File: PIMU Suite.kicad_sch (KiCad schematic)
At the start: 5 parts, among them J1 Conn_01x05, U1 Teensy4.1, U2 MICROSD_SPI_OR_SDIO_CARD

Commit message: Added impl note
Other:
- note added: "Note: Adafruit labeled this as 3V when its really 3.3V"
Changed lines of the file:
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@@
+		)
+	)
+	(text "Note: Adafruit labeled this \nas 3V when its really 3.3V"
+		(exclude_from_sim no)
+		(at 114.046 37.084 0)
+		(effects
+			(font
+				(size 1.27 1.27)
+			)
 		)
 	)

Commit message: Change pwer dist.
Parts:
- removed J1: Conn_01x05, Connector_PinHeader_1.00mm:PinHeader_1x05_P1.00mm_Vertical, symbol Connector_Generic:Conn_01x05
- added D1: LED, LED_THT:LED_D3.0mm, symbol Device:LED
- added R1: R_US, Resistor_THT:R_Axial_DIN0207_L6.3mm_D2.5mm_P7.62mm_Horizontal, symbol Device:R_US
- added TP1: 5V IN, TestPoint:TestPoint_Pad_D1.5mm, symbol Connector:TestPoint
- added TP2: GND CONN, TestPoint:TestPoint_Pad_D1.5mm, symbol Connector:TestPoint
- added TP3: I2C CLOCK, TestPoint:TestPoint_Pad_D1.5mm, symbol Connector:TestPoint
- added TP4: I2C DATA, TestPoint:TestPoint_Pad_D1.5mm, symbol Connector:TestPoint
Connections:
- net at BMP1.4 (SCK), IMU1.10 (SCL), U1.41 (19_A5_SCL): now also TP3.1
- net at IMU1.11 (SDA), U1.40 (18_A4_SDA): now also BMP1.5 (SDO), TP4.1; no longer BMP1.6 (SDI)
- net 3V3 IN: now reaches BMP1.1 (VIN), IMU1.7 (VIN), U1.46 (3V3), U2.1 (3V)
- net 3V3 IN: now also R1.2
- net GND: now reaches BMP1.3 (GND), IMU1.9 (GND), U1.1 (GND), U2.2 (GND)
- net GND: now also D1.1 (K), TP2.1
- net 5V TEENSY: now reaches U1.48 (VIN)
- net 5V TEENSY: now also TP1.1
- new net: D1.2 (A), R1.1
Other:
- note removed: "This is so we can test the teensy when not plugged into USB"
- moved on the sheet: U2

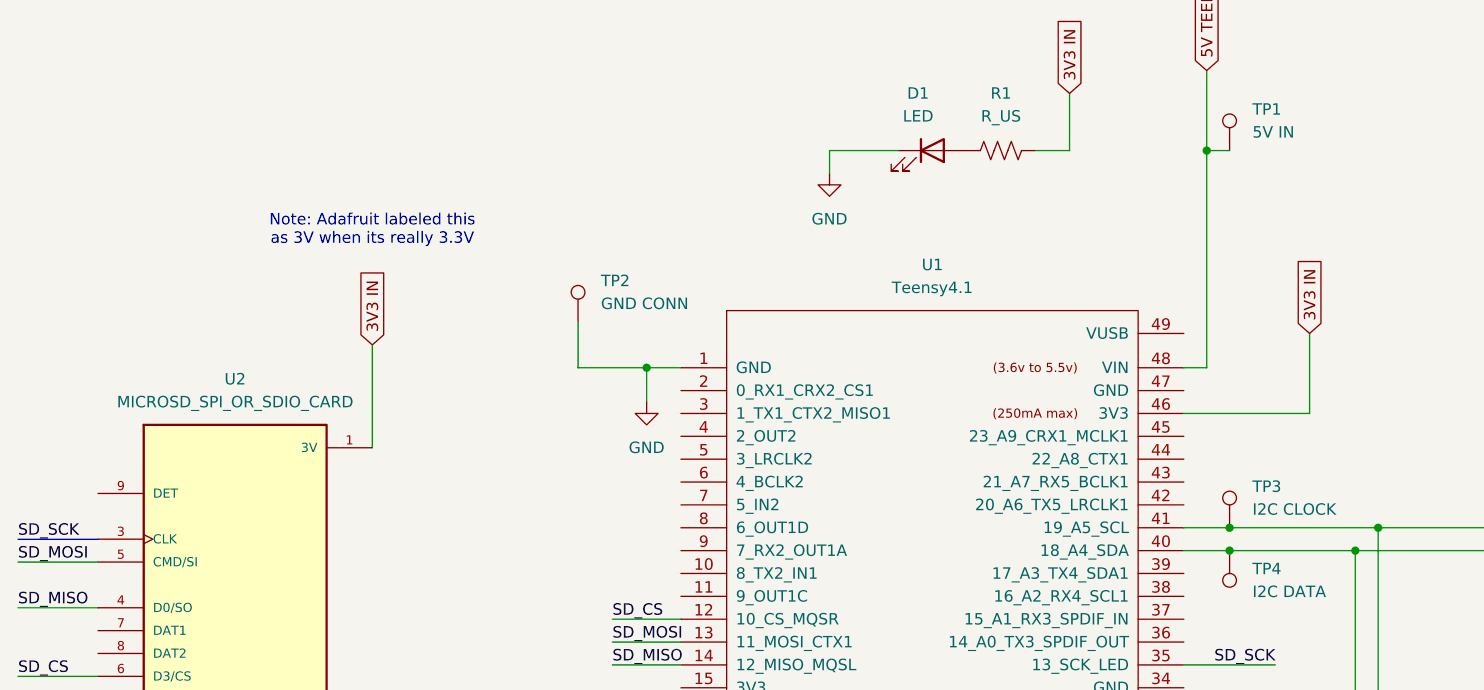
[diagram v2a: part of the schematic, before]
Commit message: Fix mistake from prev
also added a wire for the detect pin
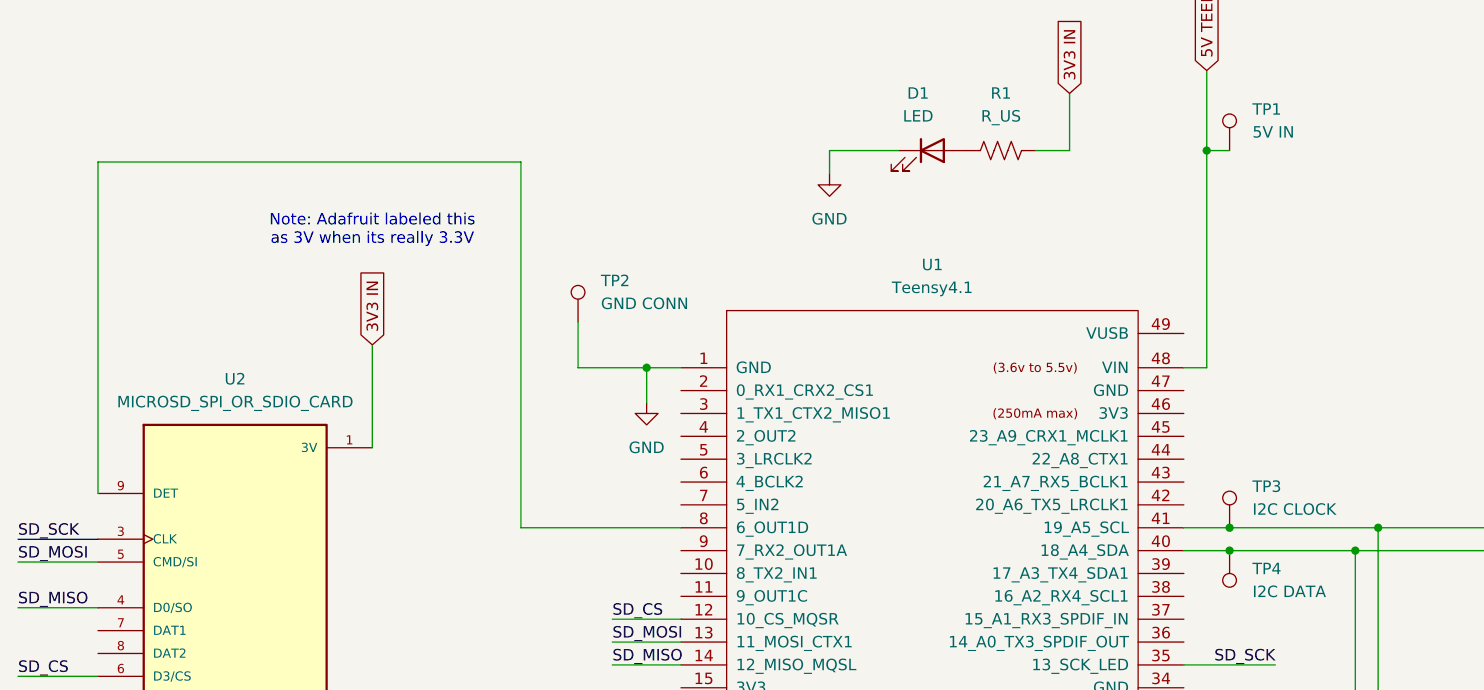
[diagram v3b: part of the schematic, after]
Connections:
- net 3V3 IN: no longer U1.46 (3V3)
- net at U1.8 (6_OUT1D): now also U2.9 (DET)
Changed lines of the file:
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@@
+	(wire
+		(pts
+			(xy 52.07 36.83) (xy 52.07 73.66)
+		)
+		(stroke
+			(width 0)
+			(type default)
+		)
+	)
 	(wire
 		(pts
@@
 	(wire
 		(pts
+			(xy 99.06 77.47) (xy 99.06 36.83)
+		)
+		(stroke
+			(width 0)
+			(type default)
+		)
+	)
+	(wire
+		(pts
 			(xy 194.31 77.47) (xy 194.31 104.14)
 		)
@@
 	(wire
 		(pts
-			(xy 172.72 64.77) (xy 186.69 64.77)
-		)
-		(stroke
-			(width 0)
-			(type default)
-		)
-	)
-	(wire
-		(pts
 			(xy 191.77 80.01) (xy 191.77 106.68)
 		)
@@
 	(wire
 		(pts
+			(xy 99.06 36.83) (xy 52.07 36.83)
+		)
+		(stroke
+			(width 0)
+			(type default)
+		)
+	)
+	(wire
+		(pts
 			(xy 43.18 86.36) (xy 52.07 86.36)
 		)
@@
 	(wire
 		(pts
+			(xy 116.84 77.47) (xy 99.06 77.47)
+		)
+		(stroke
+			(width 0)
+			(type default)
+		)
+	)
+	(wire
+		(pts
 			(xy 105.41 59.69) (xy 113.03 59.69)
 		)
@@
 		(pts
 			(xy 232.41 99.06) (xy 243.84 99.06)
-		)
-		(stroke
-			(width 0)
-			(type default)
-		)
-	)
-	(wire
-		(pts
-			(xy 186.69 55.88) (xy 186.69 64.77)
 		)
 		(stroke
@@
 			(effects
 				(font
-					(size 1.27 1.27)
-				)
-				(justify left)
-				(hide yes)
-			)
-		)
-	)
-	(global_label "3V3 IN"
-		(shape input)
-		(at 186.69 55.88 90)
-		(fields_autoplaced yes)
-		(effects
-			(font
-				(size 1.27 1.27)
-			)
-			(justify left)
-		)
-		(property "Intersheetrefs" "${INTERSHEET_REFS}"
-			(at 186.69 46.4843 90)
-			(effects
-				(font

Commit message: Nicer routes
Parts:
- added J1: Conn_01x03, Connector_PinHeader_2.00mm:PinHeader_1x03_P2.00mm_Vertical, symbol Connector_Generic:Conn_01x03
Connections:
- net GND: now also J1.3 (Pin_3)
- net SCL_LINE: now reaches BMP1.4 (SCK), IMU1.10 (SCL), TP3.1
- net SCL_LINE: now also U1.16 (24_A10_TX6_SCL2); no longer U1.41 (19_A5_SCL)
- net SDA_LINE: now reaches BMP1.5 (SDO), IMU1.11 (SDA), TP4.1
- net SDA_LINE: now also U1.17 (25_A11_RX6_SDA2); no longer U1.40 (18_A4_SDA)
- net 3V3 IN renamed +3.3V
- net +3.3V: now also J1.1 (Pin_1)
- net 5V TEENSY renamed +5V
- net +5V: now also J1.2 (Pin_2)
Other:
- moved on the sheet: D1, R1, Reference: IMU1, TP2, TP3, TP4

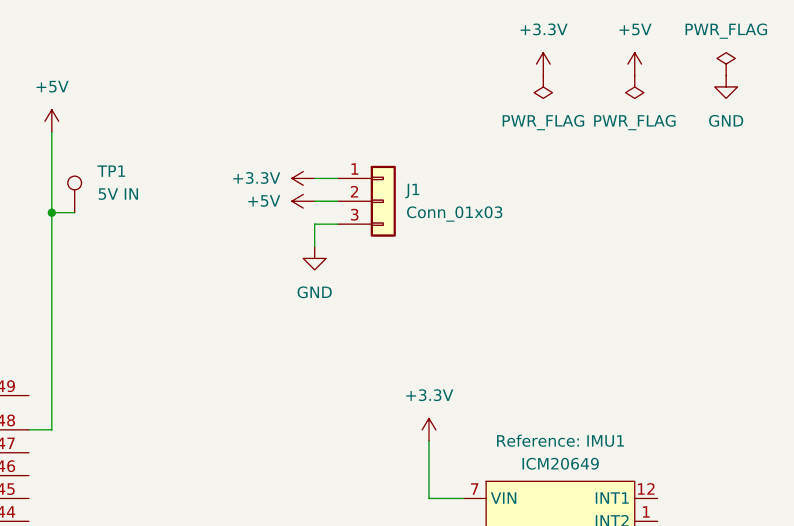
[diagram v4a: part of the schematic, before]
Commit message: New JST
also added THT resistor and LED, but the footprint will change soon
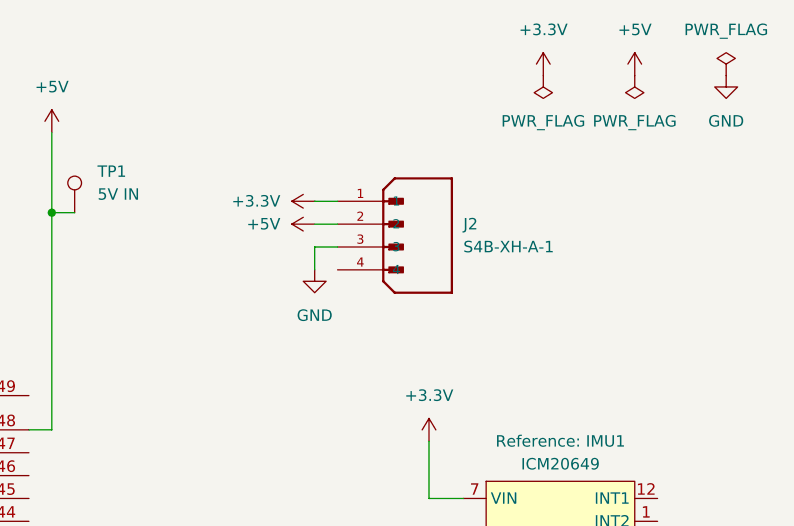
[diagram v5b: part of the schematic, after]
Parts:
- removed J1: Conn_01x03, Connector_PinHeader_2.00mm:PinHeader_1x03_P2.00mm_Vertical, symbol Connector_Generic:Conn_01x03
- added J2: S4B-XH-A-1, S4B-XH-A-1:JST_S4B-XH-A-1, symbol S4B-XH-A-1:S4B-XH-A-1
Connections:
- net +3.3V: now also J2.1
- net +5V: now also J2.2
- net GND: now also J2.3

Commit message: change footprints
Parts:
- R1: footprint Resistor_THT:R_Axial_DIN0207_L6.3mm_D2.5mm_P7.62mm_Horizontal -> Resistor_SMD:R_0805_2012Metric
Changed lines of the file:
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@@
 			)
 		)
-		(property "Footprint" "Resistor_THT:R_Axial_DIN0207_L6.3mm_D2.5mm_P7.62mm_Horizontal"
+		(property "Footprint" "Resistor_SMD:R_0805_2012Metric"
 			(at 147.574 33.274 90)
 			(effects

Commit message: Updates from team
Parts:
- D1: footprint LED_THT:LED_D3.0mm -> LED_SMD:LED_0805_2012Metric_Pad1.15x1.40mm_HandSolder
- JST1: renamed from J2; footprint S4B-XH-A-1:JST_S4B-XH-A-1 -> Connector_JST:JST_VH_B3P-VH-B_1x03_P3.96mm_Vertical; symbol S4B-XH-A-1:S4B-XH-A-1 -> Connector:Conn_01x03_Socket
- R1: footprint Resistor_SMD:R_0805_2012Metric -> Resistor_SMD:R_0805_2012Metric_Pad1.20x1.40mm_HandSolder
- renumbered U1 to TEENSY1
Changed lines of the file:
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@@
 			)
 		)
-		(property "Footprint" "Resistor_SMD:R_0805_2012Metric"
+		(property "Footprint" "Resistor_SMD:R_0805_2012Metric_Pad1.20x1.40mm_HandSolder"
 			(at 147.574 33.274 90)
 			(effects
@@
 	)
 	(symbol
-		(lib_id "S4B-XH-A-1:S4B-XH-A-1")
+		(lib_id "Connector:Conn_01x03_Socket")
 		(at 212.09 36.83 0)
 		(unit 1)
@@
 		(dnp no)
 		(fields_autoplaced yes)
-		(property "Reference" "J2"
-			(at 220.98 36.8299 0)
+		(property "Reference" "JST1"
+			(at 213.36 35.5599 0)
 			(effects
 				(font
@@
 		)
 		(property "Value" "S4B-XH-A-1"
-			(at 220.98 39.3699 0)
+			(at 213.36 38.0999 0)
 			(effects
 				(font
@@
 			)
 		)
-		(property "Footprint" "S4B-XH-A-1:JST_S4B-XH-A-1"
+		(property "Footprint" "Connector_JST:JST_VH_B3P-VH-B_1x03_P3.96mm_Vertical"
 			(at 212.09 36.83 0)
 			(effects
@@
 					(size 1.27 1.27)
 				)
-				(justify bottom)
-				(hide yes)
-			)
-		)
-		(property "Datasheet" ""
+				(hide yes)
+			)
+		)
+		(property "Datasheet" "~"
 			(at 212.09 36.83 0)
 			(effects
@@
 			)
 		)
-		(property "Description" ""
+		(property "Description" "Generic connector, single row, 01x03, script generated"
 			(at 212.09 36.83 0)
 			(effects
@@
 			)
 		)
-		(pin "4"
-		)
 		(pin "3"
 		)
@@
 			(project ""
 				(path "/f92a9e59-93af-435a-9a9e-44bda57be41a"
-					(reference "J2")
+					(reference "JST1")
 					(unit 1)
 				)
@@
 		(dnp no)
 		(fields_autoplaced yes)
-		(property "Reference" "U1"
+		(property "Reference" "TEENSY1"
 			(at 144.78 48.26 0)
 			(effects
@@
 			(project ""
 				(path "/f92a9e59-93af-435a-9a9e-44bda57be41a"
-					(reference "U1")
+					(reference "TEENSY1")
 					(unit 1)
 				)
@@
 			)
 		)
-		(property "Footprint" "LED_THT:LED_D3.0mm"
+		(property "Footprint" "LED_SMD:LED_0805_2012Metric_Pad1.15x1.40mm_HandSolder"
 			(at 139.7 34.29 0)
 			(effects

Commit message: Fix JST order
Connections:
- net +3.3V: now also JST1.3 (Pin_3); no longer JST1.1 (Pin_1)
- net GND: now also JST1.1 (Pin_1); no longer JST1.3 (Pin_3)
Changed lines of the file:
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@@
-	(wire
-		(pts
-			(xy 204.47 39.37) (xy 204.47 41.91)
-		)
-		(stroke
-			(width 0)
-			(type default)
-		)
-	)
 	(wire
 		(pts
@@
 	(symbol
 		(lib_id "power:GND")
-		(at 204.47 41.91 0)
+		(at 204.47 34.29 270)
 		(unit 1)
 		(exclude_from_sim no)
@@
 		(fields_autoplaced yes)
 		(property "Reference" "#PWR06"
-			(at 204.47 48.26 0)
+			(at 198.12 34.29 0)
 			(effects
 				(font
@@
 		)
 		(property "Value" "GND"
-			(at 204.47 46.99 0)
+			(at 203.2 30.48 90)
 			(effects
 				(font
@@
 		)
 		(property "Footprint" ""
-			(at 204.47 41.91 0)
+			(at 204.47 34.29 0)
 			(effects
 				(font
@@
 		)
 		(property "Datasheet" ""
-			(at 204.47 41.91 0)
+			(at 204.47 34.29 0)
 			(effects
 				(font
@@
 		)
 		(property "Description" "Power symbol creates a global label with name \"GND\" , ground"
-			(at 204.47 41.91 0)
+			(at 204.47 34.29 0)
 			(effects
 				(font
@@
 	(symbol
 		(lib_id "power:+3.3V")
-		(at 204.47 34.29 90)
+		(at 204.47 39.37 90)
 		(unit 1)
 		(exclude_from_sim no)
@@
 		(fields_autoplaced yes)
 		(property "Reference" "#PWR011"
-			(at 208.28 34.29 0)
+			(at 208.28 39.37 0)
 			(effects
 				(font
@@
 		)
 		(property "Value" "+3.3V"
-			(at 200.66 34.2899 90)
+			(at 200.66 39.3699 90)
 			(effects
 				(font
@@
 		)
 		(property "Footprint" ""
-			(at 204.47 34.29 0)
+			(at 204.47 39.37 0)
 			(effects
 				(font
@@
 		)
 		(property "Datasheet" ""
-			(at 204.47 34.29 0)
+			(at 204.47 39.37 0)
 			(effects
 				(font
@@
 		)
 		(property "Description" "Power symbol creates a global label with name \"+3.3V\""
-			(at 204.47 34.29 0)
-			(effects
-				(font
+			(at 204.47 39.37 0)
+			(effects
+				(font
